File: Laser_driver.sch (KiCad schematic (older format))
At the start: 0 parts

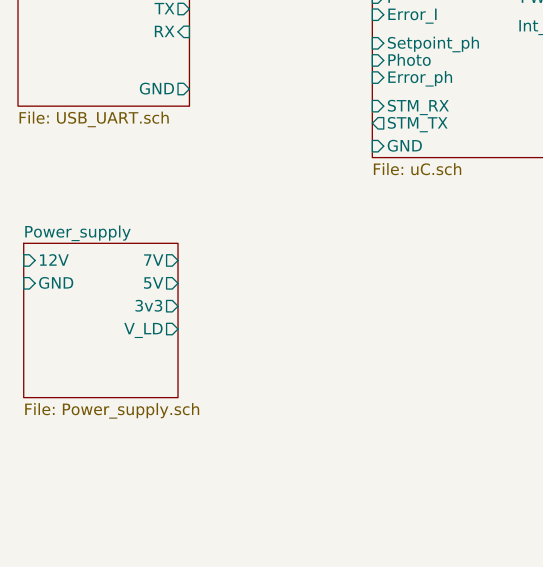
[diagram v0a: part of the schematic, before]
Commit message: Removed MC34063 added DC/DC module & +-5V LDO
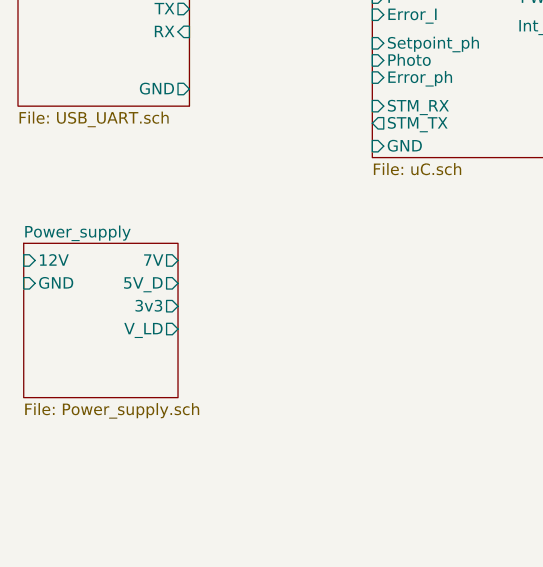
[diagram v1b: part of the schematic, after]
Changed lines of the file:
@@
 F3 "GND" I L 1625 2625 50
 F4 "7V" O R 2300 2525 50
-F5 "5V" O R 2300 2625 50
-F6 "3v3" O R 2300 2725 50
-F7 "V_LD" O R 2300 2825 50
+F5 "3v3" O R 2300 2725 50
+F6 "V_LD" O R 2300 2825 50
+F7 "5V_D" O R 2300 2625 50
 $EndSheet
 $Sheet

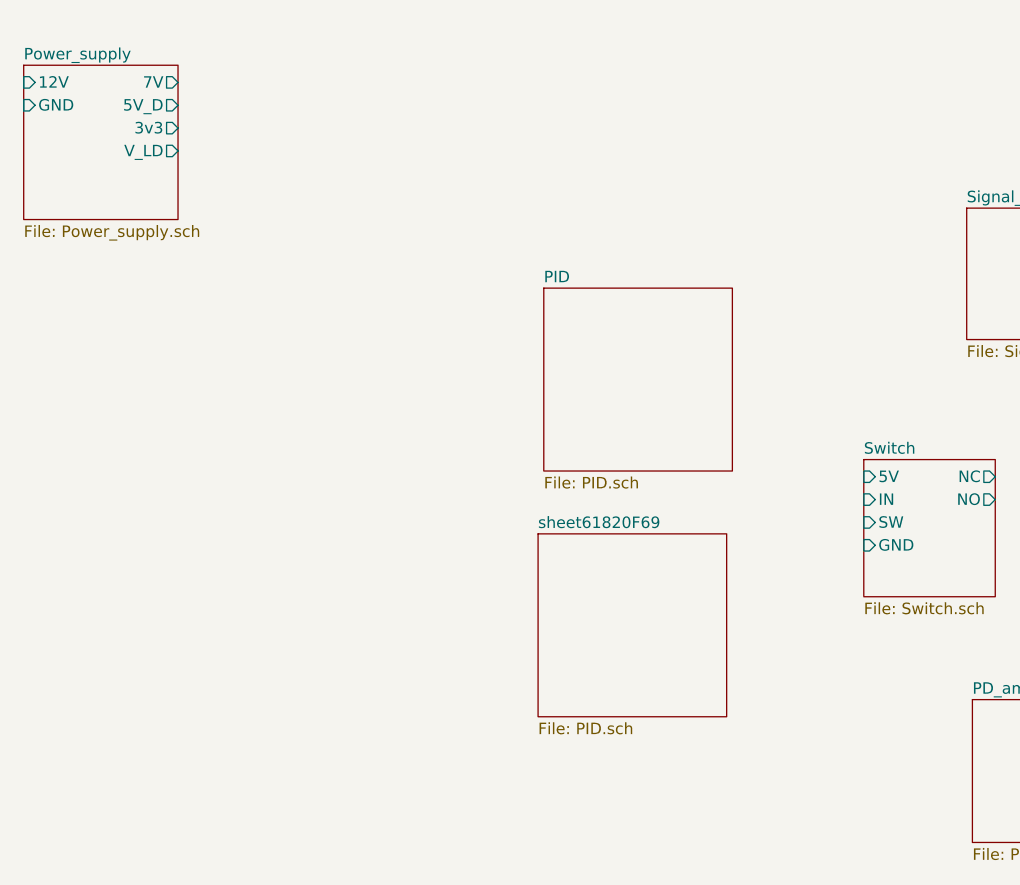
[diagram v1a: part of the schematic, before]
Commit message: Added PIDs blocks
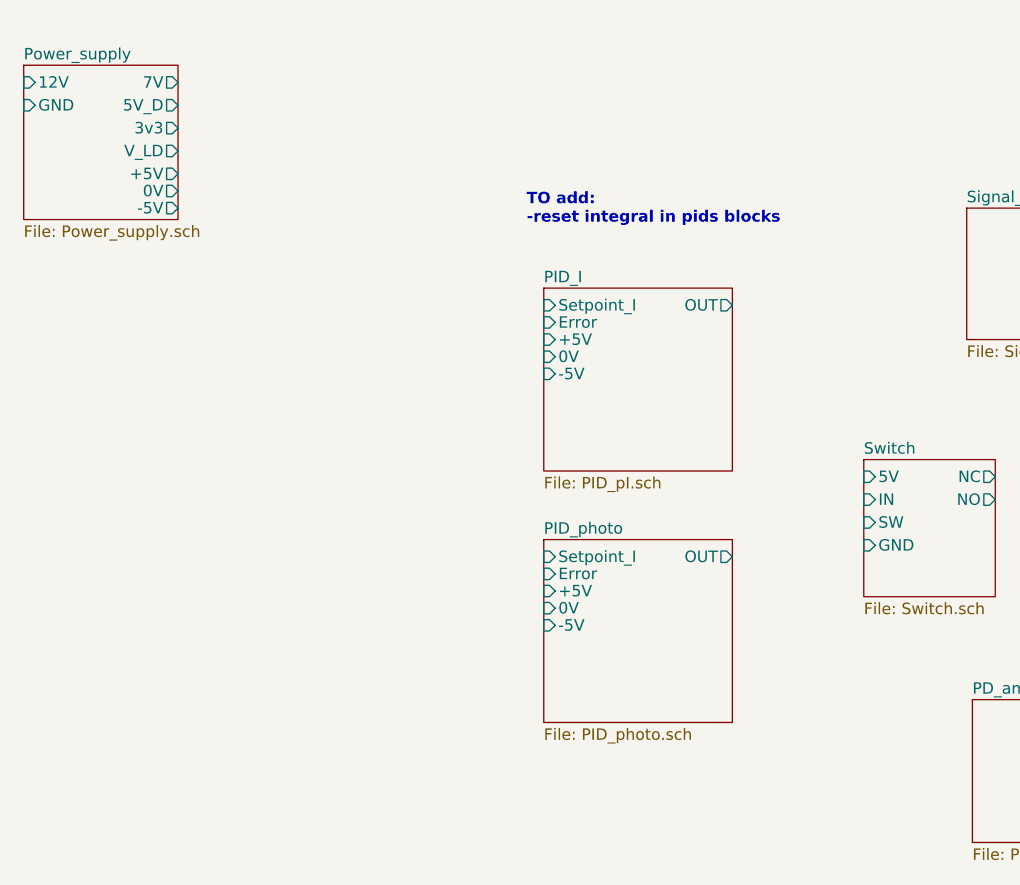
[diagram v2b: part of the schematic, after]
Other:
- note added: "TO add:\n-reset integral in pids blocks\n"
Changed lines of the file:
@@
 F6 "V_LD" O R 2300 2825 50
 F7 "5V_D" O R 2300 2625 50
+F8 "+5V" O R 2300 2925 50
+F9 "-5V" O R 2300 3075 50
+F10 "0V" O R 2300 3000 50
 $EndSheet
 $Sheet
@@
 $EndSheet
 $Sheet
-S 3900 3425 825  800
-U 619B51F3
-F0 "PID" 50
-F1 "PID.sch" 50
-$EndSheet
-$Sheet
-S 3875 4500 825  800
-U 61820F6B
-F0 "sheet61820F69" 50
-F1 "PID.sch" 50
-$EndSheet
-$Sheet
 S 5775 5225 625  625
 U 61838EBB
@@
 F1 "Signal_conditioner.sch" 50
 $EndSheet
+$Sheet
+S 3900 4525 825  800
+U 61A28785
+F0 "PID_photo" 50
+F1 "PID_photo.sch" 50
+F2 "Setpoint_I" I L 3900 4600 50
+F3 "Error" I L 3900 4675 50
+F4 "+5V" I L 3900 4750 50
+F5 "-5V" I L 3900 4900 50
+F6 "0V" I L 3900 4825 50
+F7 "OUT" O R 4725 4600 50
+$EndSheet
+$Sheet
+S 3900 3425 825  800
+U 619B51F3
+F0 "PID_I" 50
+F1 "PID_pI.sch" 50
+F2 "Setpoint_I" I L 3900 3500 50
+F3 "Error" I L 3900 3575 50
+F4 "+5V" I L 3900 3650 50
+F5 "-5V" I L 3900 3800 50
+F6 "0V" I L 3900 3725 50
+F7 "OUT" O R 4725 3500 50
+$EndSheet
+Text Notes 3825 3150 0    50   ~ 10
+TO add:\n-reset integral in pids blocks\n
 $EndSCHEMATC

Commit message: Added jumpers to PID blocks
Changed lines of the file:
@@
-$EndSheet
-$Sheet
-S 3900 4525 825  800
-U 61A28785
-F0 "PID_photo" 50
-F1 "PID_photo.sch" 50
-F2 "Setpoint_I" I L 3900 4600 50
-F3 "Error" I L 3900 4675 50
-F4 "+5V" I L 3900 4750 50
-F5 "-5V" I L 3900 4900 50
-F6 "0V" I L 3900 4825 50
-F7 "OUT" O R 4725 4600 50
 $EndSheet
 $Sheet
@@
 Text Notes 3825 3150 0    50   ~ 10
 TO add:\n-reset integral in pids blocks\n
+$Sheet
+S 3900 4750 825  800
+U 61A63B19
+F0 "PID_photo" 50
+F1 "PID_photo.sch" 50
+F2 "Setpoint_I" I L 3900 4825 50
+F3 "Error" I L 3900 4900 50
+F4 "+5V" I L 3900 4975 50
+F5 "-5V" I L 3900 5125 50
+F6 "0V" I L 3900 5050 50
+F7 "OUT" O R 4725 4825 50
+$EndSheet
 $EndSCHEMATC

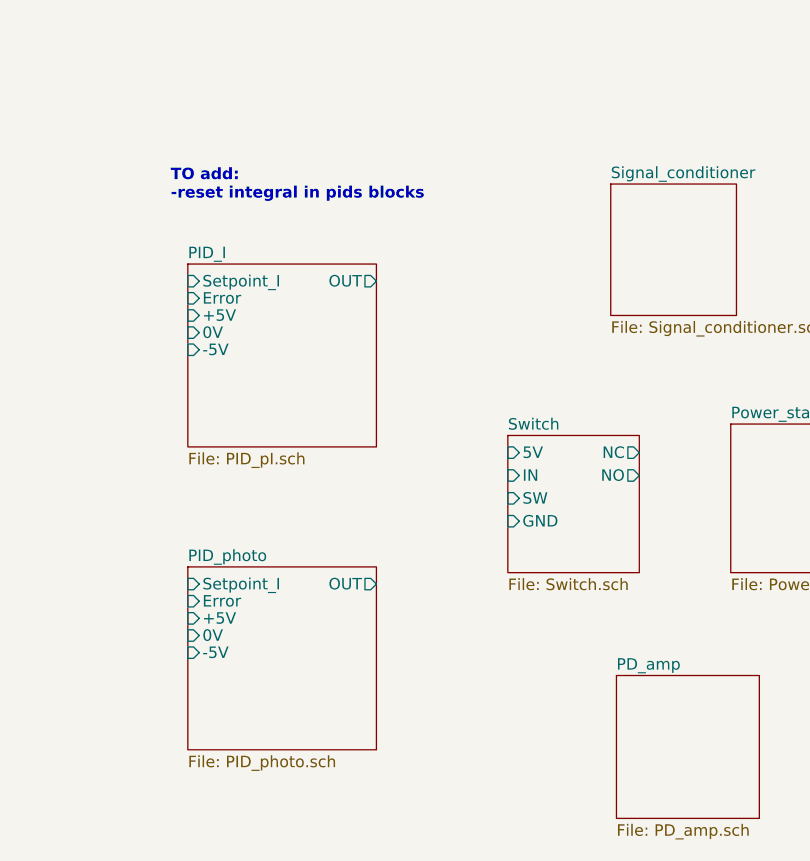
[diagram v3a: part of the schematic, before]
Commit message: Added integrator reset, fixed Switch.sch
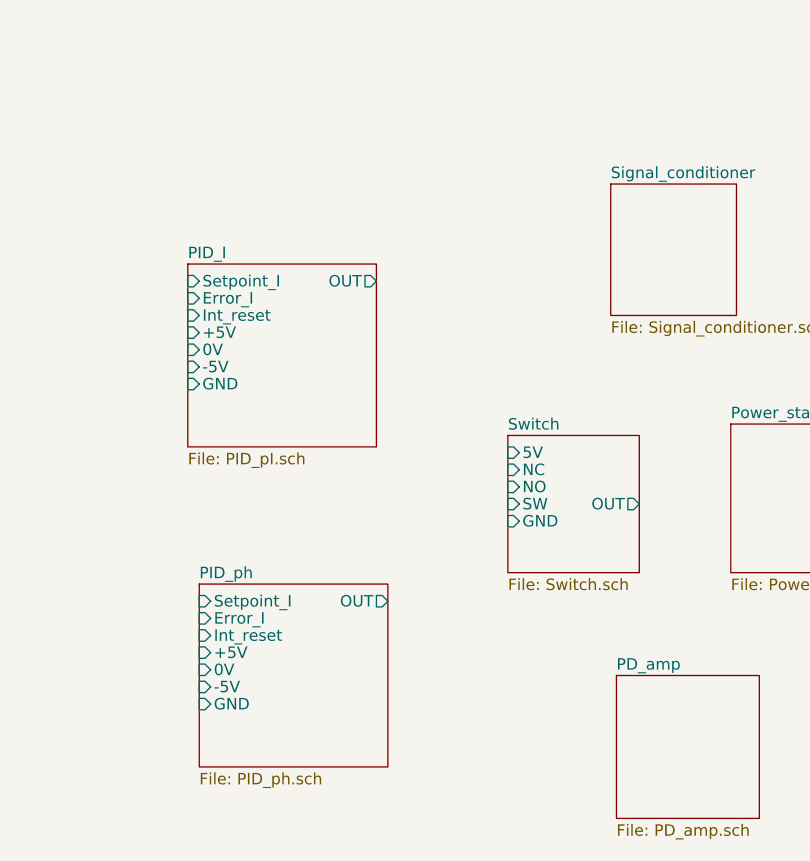
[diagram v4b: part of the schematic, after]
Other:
- note removed: "TO add:\n-reset integral in pids blocks\n"
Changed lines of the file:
@@
 F0 "Switch" 50
 F1 "Switch.sch" 50
-F2 "NC" O R 5875 4250 50
-F3 "NO" O R 5875 4350 50
-F4 "IN" I L 5300 4350 50
-F5 "5V" I L 5300 4250 50
-F6 "GND" I L 5300 4550 50
-F7 "SW" I L 5300 4450 50
+F2 "5V" I L 5300 4250 50
+F3 "GND" I L 5300 4550 50
+F4 "SW" I L 5300 4475 50
+F5 "NC" I L 5300 4325 50
+F6 "NO" I L 5300 4400 50
+F7 "OUT" O R 5875 4475 50
 $EndSheet
 $Sheet
@@
 F1 "PID_pI.sch" 50
 F2 "Setpoint_I" I L 3900 3500 50
-F3 "Error" I L 3900 3575 50
-F4 "+5V" I L 3900 3650 50
-F5 "-5V" I L 3900 3800 50
-F6 "0V" I L 3900 3725 50
-F7 "OUT" O R 4725 3500 50
+F3 "+5V" I L 3900 3725 50
+F4 "-5V" I L 3900 3875 50
+F5 "0V" I L 3900 3800 50
+F6 "OUT" O R 4725 3500 50
+F7 "Error_I" I L 3900 3575 50
+F8 "GND" I L 3900 3950 50
+F9 "Int_reset" I L 3900 3650 50
 $EndSheet
-Text Notes 3825 3150 0    50   ~ 10
-TO add:\n-reset integral in pids blocks\n
 $Sheet
-S 3900 4750 825  800
-U 61A63B19
-F0 "PID_photo" 50
-F1 "PID_photo.sch" 50
-F2 "Setpoint_I" I L 3900 4825 50
-F3 "Error" I L 3900 4900 50
-F4 "+5V" I L 3900 4975 50
-F5 "-5V" I L 3900 5125 50
-F6 "0V" I L 3900 5050 50
-F7 "OUT" O R 4725 4825 50
+S 3950 4825 825  800
+U 619C995F
+F0 "PID_ph" 50
+F1 "PID_ph.sch" 50
+F2 "Setpoint_I" I L 3950 4900 50
+F3 "+5V" I L 3950 5125 50
+F4 "-5V" I L 3950 5275 50
+F5 "0V" I L 3950 5200 50
+F6 "OUT" O R 4775 4900 50
+F7 "Error_I" I L 3950 4975 50
+F8 "GND" I L 3950 5350 50
+F9 "Int_reset" I L 3950 5050 50
 $EndSheet
 $EndSCHEMATC

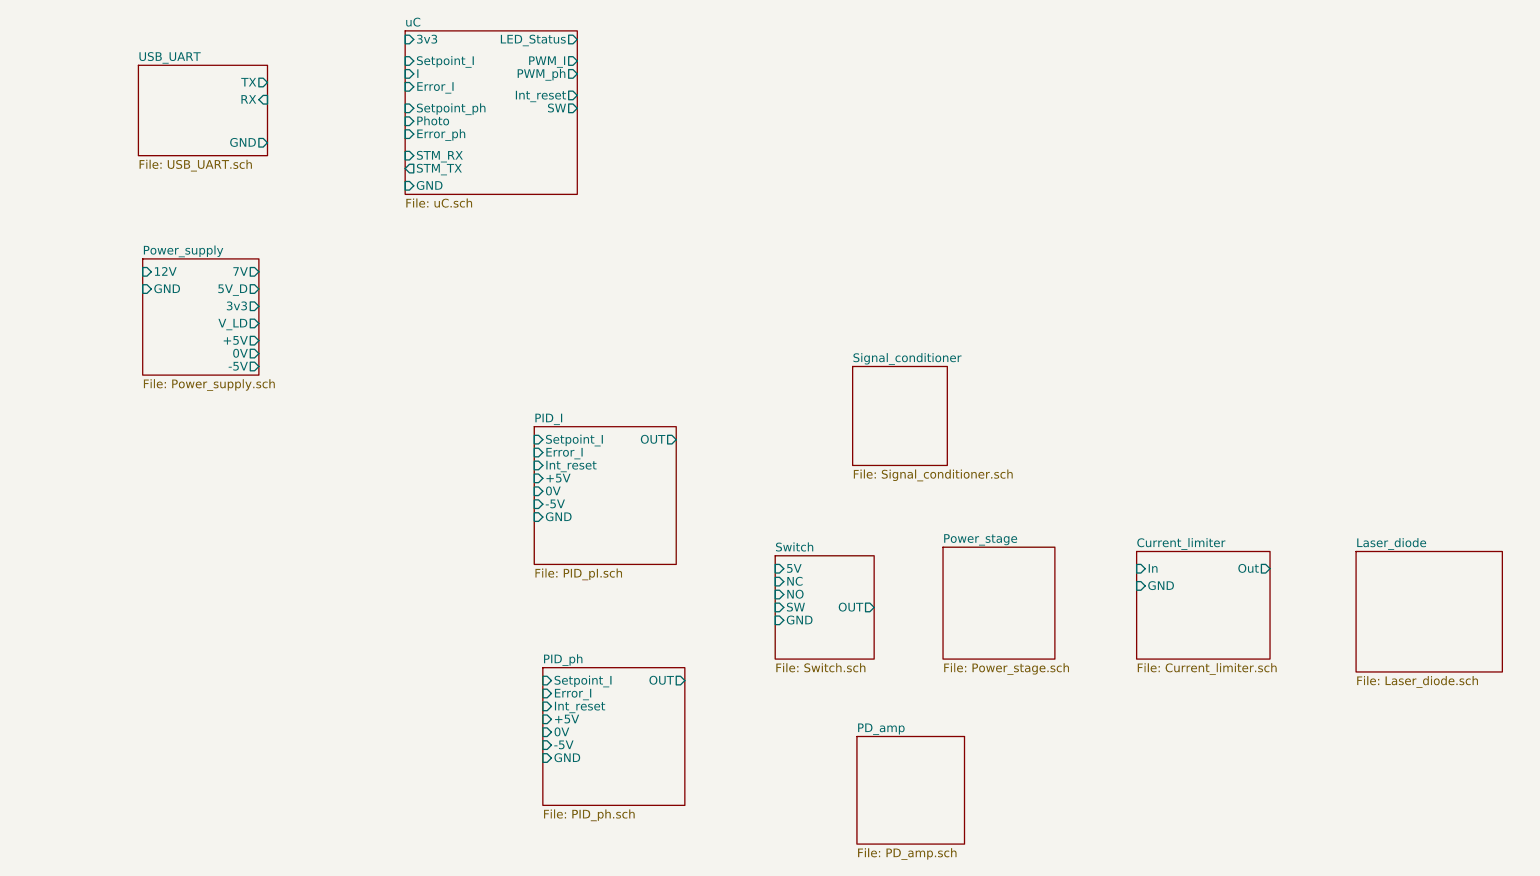
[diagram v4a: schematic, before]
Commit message: Added laser diode, power stage, connecting block in progress
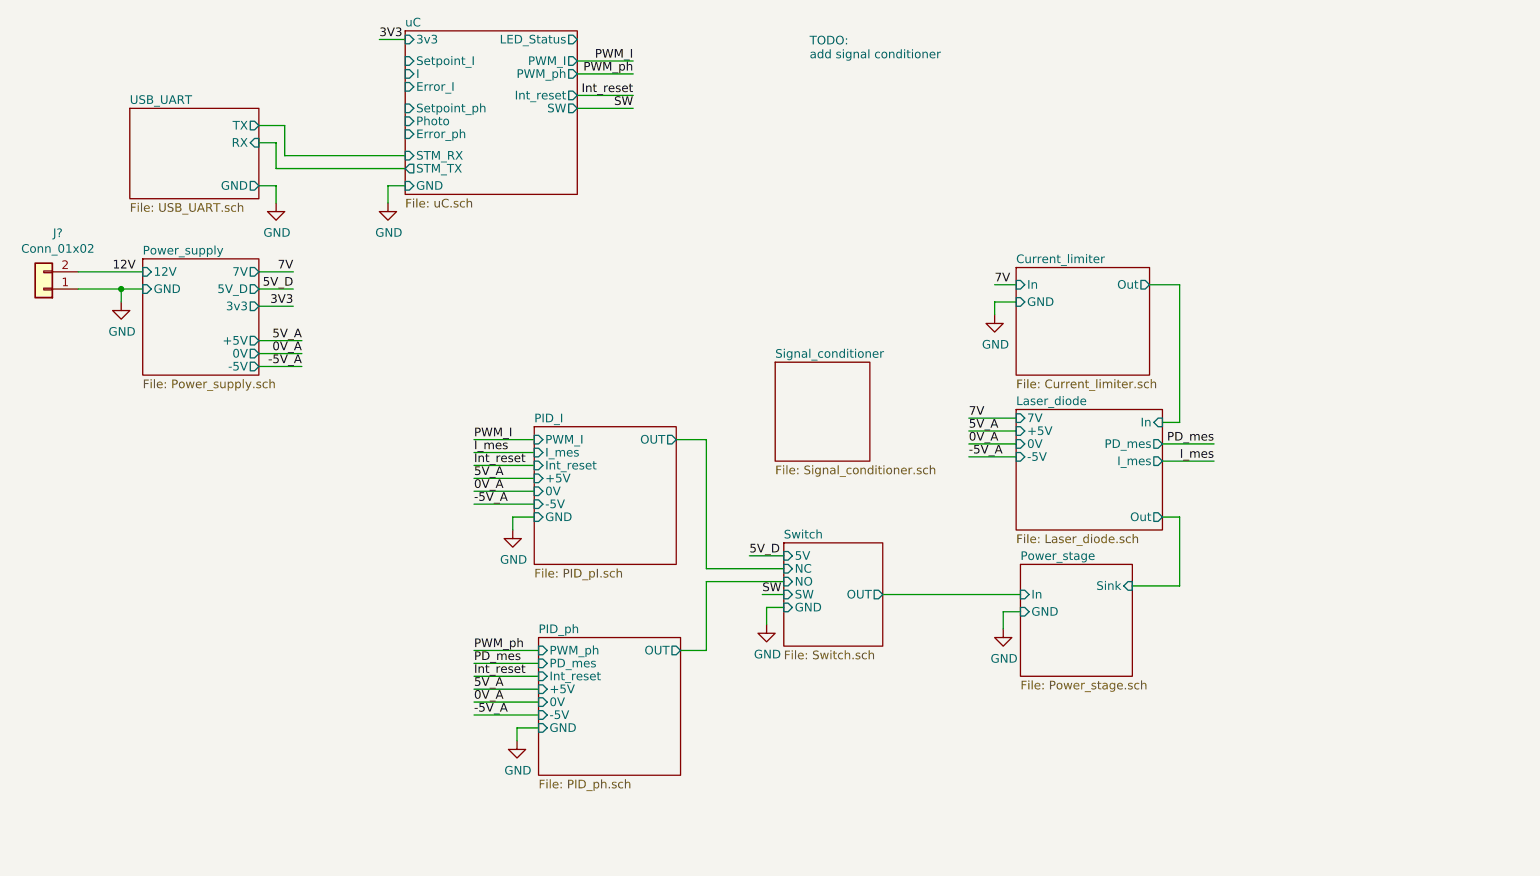
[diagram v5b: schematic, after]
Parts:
- added J?: Conn_01x02, symbol Connector_Generic:Conn_01x02
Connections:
- new net 12V: J?.2 (Pin_2)
- new net GND: J?.1 (Pin_1)
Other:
- note added: "TODO:\nadd signal conditioner\n"
